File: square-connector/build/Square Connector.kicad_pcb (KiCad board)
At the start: 2 copper layers, 30 x 61 mm, 7 parts

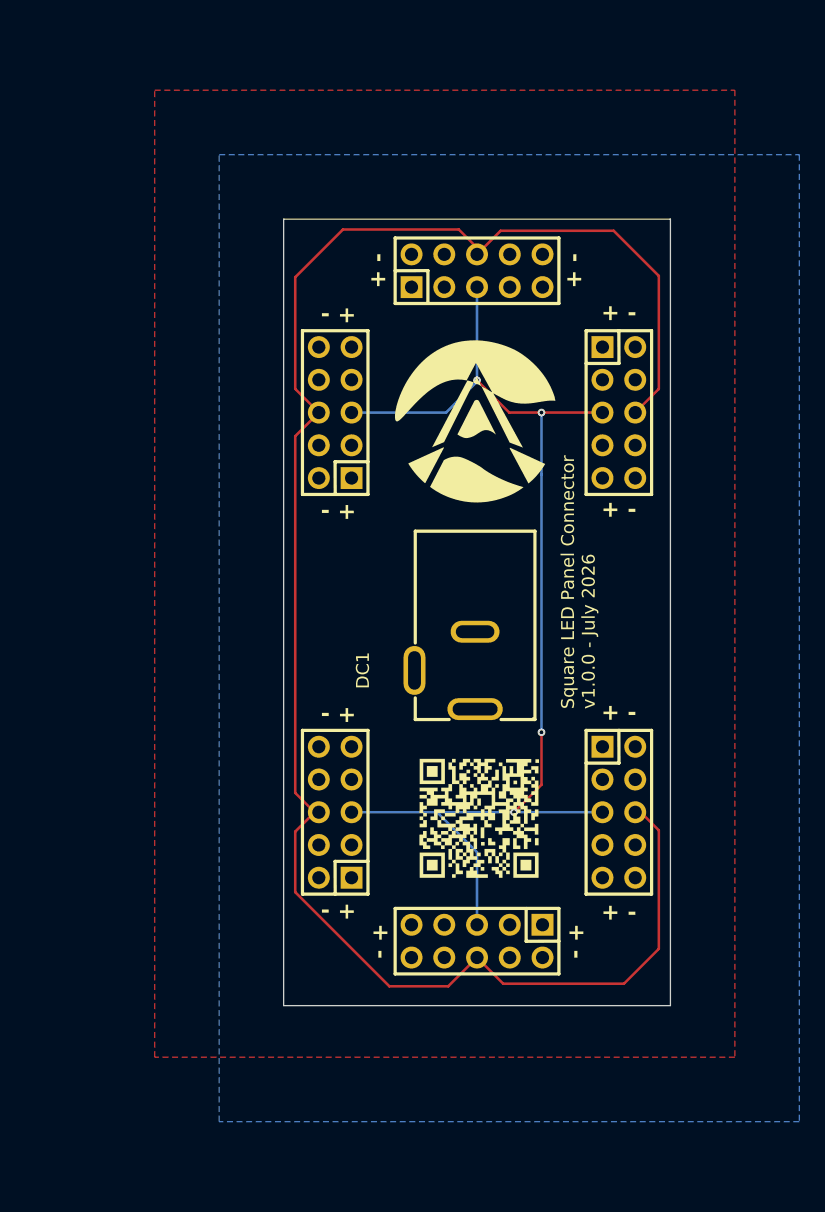
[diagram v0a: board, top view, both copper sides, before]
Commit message: Working square connector
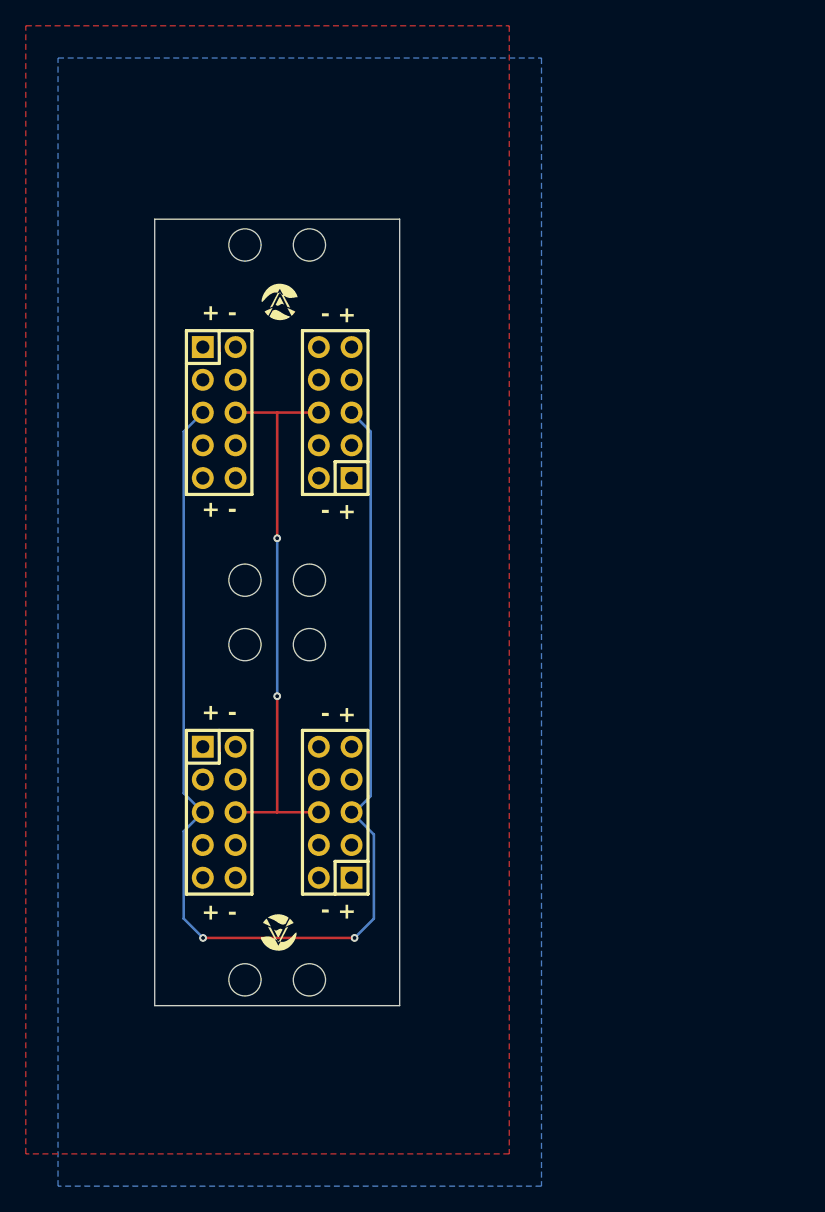
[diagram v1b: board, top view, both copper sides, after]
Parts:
- removed DC1: PJ-002BH, Schrune:PJ_002BH
- removed H1, H2: PZ2.54-2X5P-H25, Schrune:PZ2_54_2X5P_H25
- moved H3 31.0 mm to (95.0, 115.0)
- moved H4 31.0 mm to (95.0, 146.0)
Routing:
- net /pwm_warm: track 140.9 -> 43.9 mm, vias 0 -> 2
- net /pwm_cool: track 90.2 -> 98.4 mm, vias 4 -> 2
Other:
- board size 30 x 61 mm -> 19 x 61 mm
- board text added: "Square LED Panel Connector v1.0.1 - July 2026"
- board text removed: "Square LED Panel Connector v1.0.0 - July 2026"
